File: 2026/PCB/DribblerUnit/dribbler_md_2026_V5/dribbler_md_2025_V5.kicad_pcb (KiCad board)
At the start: 2 copper layers, 82 x 26 mm, 126 parts, among them J2 Conn_01x04_Pin, J3 Conn_01x02_Pin, J4 Conn_01x07_Pin, J5 Conn_01x03_Pin, J6 Conn_01x02_Pin, J7 Conn_01x02_Pin, J8 Conn_01x02_Socket, SW2 SW_MEC_5E, SW4 SW_MEC_5E, U1 MAX3051, U2 STS8DN3LLH5, U3 STS8DN3LLH5, U4 DRV8701, U5 STM32F446RETx, Y1 Crystal_GND2

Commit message: シルク修正
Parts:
- removed J5: Conn_01x03_Pin, Connector_Molex:Molex_SPOX_5268-03A_1x03_P2.50mm_Horizontal
- removed J6, J7: Conn_01x02_Pin, Connector_JST:JST_PH_S2B-PH-K_1x02_P2.00mm_Horizontal
- added J1: Conn_01x05_Pin, Connector_Molex:Molex_SPOX_5268-05A_1x05_P2.50mm_Horizontal, F.Cu at (216.4, 86.1)
- added J4: Conn_01x04_Pin, Connector_JST:JST_PH_S4B-PH-K_1x04_P2.00mm_Horizontal, F.Cu at (200.9, 85.8)
- moved J2 1.74 mm to (189.9, 85.8)
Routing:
- net CANH: track 5.67 -> 40.6 mm, vias 0 -> 1
- net CANL: track 5.65 -> 39.0 mm
- net Net-(J1-Pin_3): track 0.00 -> 4.52 mm
- net GND_log: track 57.2 -> 54.8 mm, vias 83 -> 77
- net Net-(J4-Pin_1): track 4.75 -> 3.52 mm
- net ENC_1: track 21.5 -> 20.4 mm
- net BS_OUT: track 4.64 -> 5.49 mm
- net BS_IN: track 20.5 -> 21.2 mm
- net ENC_POWER: track 13.8 -> 14.5 mm
- removed copper zone on B.Cu, net Net-(J1-Pin_3)
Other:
- board text added: "20V"
- board text added: "6V5"
- board text added: "Dribbler Driver"
- board text added: "Rot_No.17DEC2026"
- board text added: "SSL 2026"
- board text added: "V26.1.1 Tsukigake"
- board text removed: "18V"
- board text removed: "6.5V"
- board text removed: "Dribbler Driver V4"
- board text removed: "H.S.O.S.6"
- board text removed: "Rot_No.25MAR2025"
- board text removed: "SSL 2025"
- board text removed: "Tsukigake"

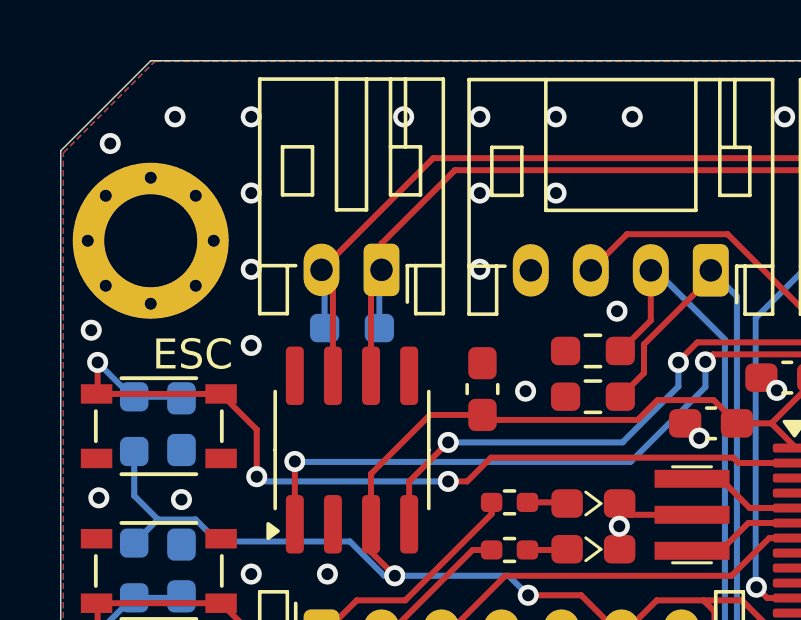
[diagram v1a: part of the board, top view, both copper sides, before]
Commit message: フットプリント変更
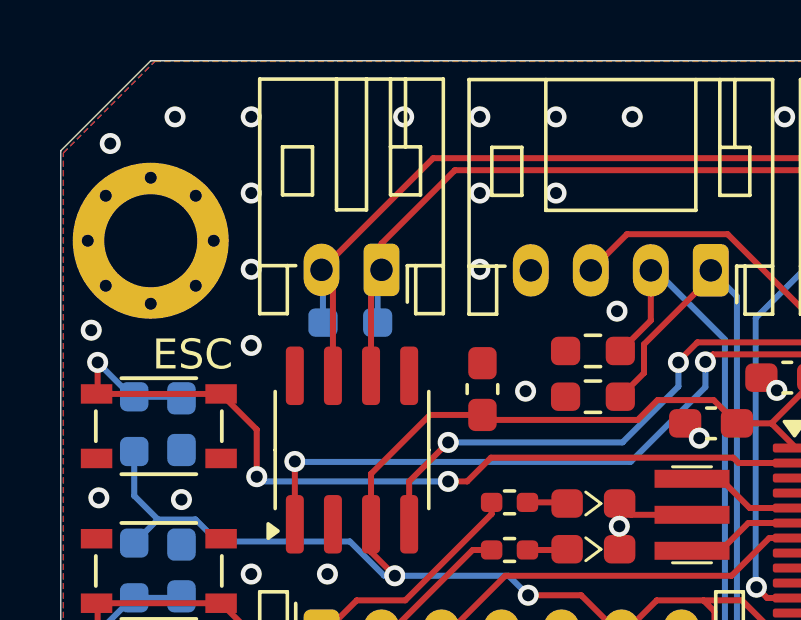
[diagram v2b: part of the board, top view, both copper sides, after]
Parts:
- moved G*** 0.86 mm to (188.2, 89.9)
- moved R5 0.19 mm to (177.9, 87.5)
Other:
- board text added: "Git_No.17fe4d9b004896a47c4d5 713bca41b0264ba8419"
- board text added: "Tsukigake"
- board text removed: "Git_No.b4d8959efe4f0d2e1a653 4d177145607de7a49e6"

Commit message: 位置修正
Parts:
- moved G*** 0.43 mm to (188.7, 89.8)
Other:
- board text added: "Dribbler Driver V26.1.1"
- board text added: "EYE OF HORUS 465"
- board text removed: "Dribbler Driver"
- board text removed: "V26.1.1 Tsukigake"

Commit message: 製造ファイル出力
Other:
- board text added: "Rot_No.17DEC2026-26-1-1"
- board text removed: "Rot_No.17DEC2026"
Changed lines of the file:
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@@
 	)
 	(gr_text "Git_No.17fe4d9b004896a47c4d5\n       713bca41b0264ba8419"
-		(at 194.100523 95.766421 0)
+		(at 194.09368 96.144996 0)
 		(layer "B.SilkS")
 		(effects
@@
 		)
 	)
-	(gr_text "Rot_No.17DEC2026"
-		(at 194.405323 93.175621 0)
+	(gr_text "Rot_No.17DEC2026-26-1-1"
+		(at 194.39848 93.554196 0)
 		(layer "B.SilkS")
 		(effects

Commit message: 最終確認完了
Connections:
- REG1 pad 1: GND_log -> 6.5V_main
- REG1 pad 3: 6.5V_main -> GND_log
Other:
- board text added: "Rot_No.17DEC2025-26-1-1"
- board text removed: "Rot_No.17DEC2026-26-1-1"
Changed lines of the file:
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@@
 			(layers "F.Cu" "F.Mask" "F.Paste")
 			(roundrect_rratio 0.25)
-			(net 2 "GND_log")
+			(net 18 "6.5V_main")
 			(pinfunction "VIN")
 			(pintype "input")
@@
 			(layers "F.Cu" "F.Mask" "F.Paste")
 			(roundrect_rratio 0.25)
-			(net 18 "6.5V_main")
+			(net 2 "GND_log")
 			(pinfunction "GND")
 			(pintype "output")
@@
 		)
 	)
-	(gr_text "Rot_No.17DEC2026-26-1-1"
+	(gr_text "Rot_No.17DEC2025-26-1-1"
 		(at 194.39848 93.554196 0)
 		(layer "B.SilkS")
